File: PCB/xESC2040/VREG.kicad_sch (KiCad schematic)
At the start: 3 parts, among them U5 XC6220B331MR

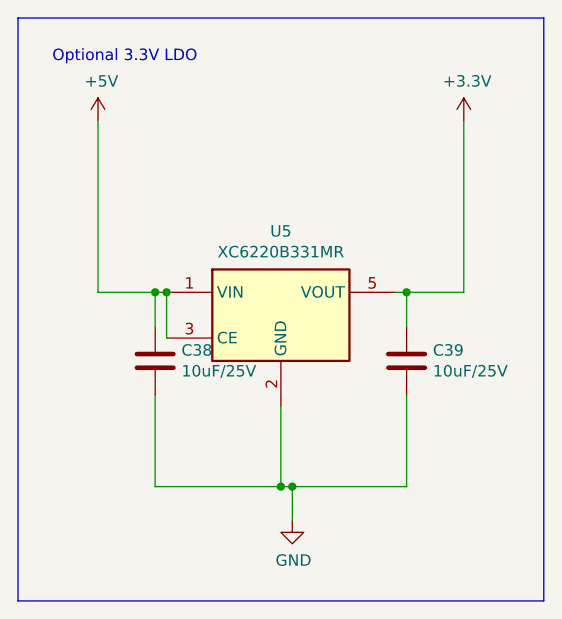
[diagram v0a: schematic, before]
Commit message: added CAN, WIP
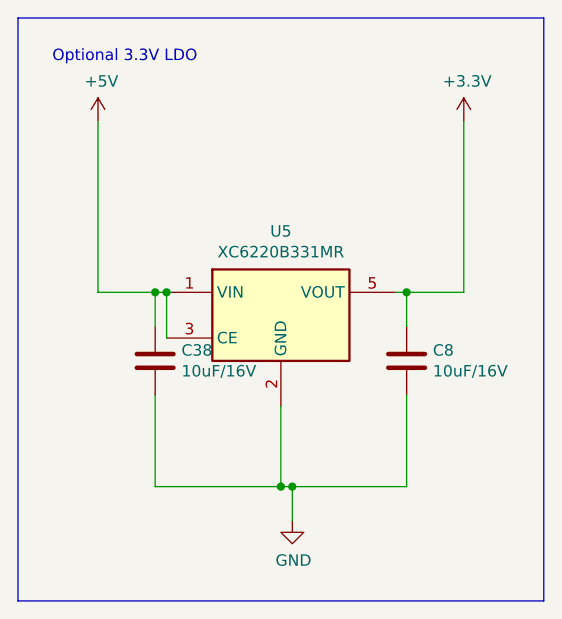
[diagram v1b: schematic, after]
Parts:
- removed C39: 10uF/25V, Capacitor_SMD:C_1206_3216Metric, symbol Device:C
- added C8: 10uF/16V, Capacitor_SMD:C_0603_1608Metric, symbol Device:C
- C38: value 10uF/25V -> 10uF/16V; footprint Capacitor_SMD:C_1206_3216Metric -> Capacitor_SMD:C_0603_1608Metric; Digikey 1276-1075-1-ND -> 1276-1096-2-ND; Part Number CL31A106KAHNNNE -> CL21A106KOQNNNE; Stock_PN C-1206-10uF-25V-X5R -> C-0603-10uF-16V
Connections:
- net +3V3: now also C8.1
- net GND: now also C8.2
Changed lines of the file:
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@@
       (effects (font (size 1.27 1.27)) (justify left))
     )
-    (property "Value" "10uF/25V" (id 1) (at 179.451 98.933 0)
+    (property "Value" "10uF/16V" (id 1) (at 179.451 98.933 0)
       (effects (font (size 1.27 1.27)) (justify left))
     )
-    (property "Footprint" "Capacitor_SMD:C_1206_3216Metric" (id 2) (at 177.4952 101.6 0)
+    (property "Footprint" "Capacitor_SMD:C_0603_1608Metric" (id 2) (at 177.4952 101.6 0)
       (effects (font (size 1.27 1.27)) hide)
     )
@@
       (effects (font (size 1.27 1.27)) hide)
     )
-    (property "Digikey" "1276-1075-1-ND" (id 4) (at 176.53 97.79 0)
+    (property "Digikey" "1276-1096-2-ND" (id 4) (at 176.53 97.79 0)
       (effects (font (size 1.27 1.27)) hide)
     )
-    (property "Part Number" "CL31A106KAHNNNE" (id 5) (at 176.53 97.79 0)
+    (property "Part Number" "CL21A106KOQNNNE" (id 5) (at 176.53 97.79 0)
       (effects (font (size 1.27 1.27)) hide)
     )
-    (property "Stock_PN" "C-1206-10uF-25V-X5R" (id 6) (at 176.53 97.79 0)
+    (property "Stock_PN" "C-0603-10uF-16V" (id 6) (at 176.53 97.79 0)
       (effects (font (size 1.27 1.27)) hide)
     )
@@
     )
     (pin "1")
-  )
-  (symbol (lib_id "Device:C") (at 204.47 97.79 0) (unit 1)
-    (in_bom yes) (on_board yes)
-    (property "Reference" "C39" (id 0) (at 207.391 96.6216 0)
-      (effects (font (size 1.27 1.27)) (justify left))
-    )
-    (property "Value" "10uF/25V" (id 1) (at 207.391 98.933 0)
-      (effects (font (size 1.27 1.27)) (justify left))
-    )
-    (property "Footprint" "Capacitor_SMD:C_1206_3216Metric" (id 2) (at 205.4352 101.6 0)
-      (effects (font (size 1.27 1.27)) hide)
-    )
-    (property "Datasheet" "~" (id 3) (at 204.47 97.79 0)
-      (effects (font (size 1.27 1.27)) hide)
-    )
-    (property "Digikey" "1276-1075-1-ND" (id 4) (at 204.47 97.79 0)
-      (effects (font (size 1.27 1.27)) hide)
-    )
-    (property "Part Number" "CL31A106KAHNNNE" (id 5) (at 204.47 97.79 0)
-      (effects (font (size 1.27 1.27)) hide)
-    )
-    (property "Stock_PN" "C-1206-10uF-25V-X5R" (id 6) (at 204.47 97.79 0)
-      (effects (font (size 1.27 1.27)) hide)
-    )
-    (pin "1")
-    (pin "2")
   )
   (symbol (lib_id "Regulator_Linear:XC6220B331MR") (at 190.5 92.71 0) (unit 1)
@@
     (pin "5")
   )
+  (symbol (lib_id "Device:C") (at 204.47 97.79 0) (unit 1)
+    (in_bom yes) (on_board yes)
+    (property "Reference" "C8" (id 0) (at 207.391 96.6216 0)
+      (effects (font (size 1.27 1.27)) (justify left))
+    )
+    (property "Value" "10uF/16V" (id 1) (at 207.391 98.933 0)
+      (effects (font (size 1.27 1.27)) (justify left))
+    )
+    (property "Footprint" "Capacitor_SMD:C_0603_1608Metric" (id 2) (at 205.4352 101.6 0)
+      (effects (font (size 1.27 1.27)) hide)
+    )
+    (property "Datasheet" "~" (id 3) (at 204.47 97.79 0)
+      (effects (font (size 1.27 1.27)) hide)
+    )
+    (property "Digikey" "1276-1096-2-ND" (id 4) (at 204.47 97.79 0)
+      (effects (font (size 1.27 1.27)) hide)
+    )
+    (property "Part Number" "CL21A106KOQNNNE" (id 5) (at 204.47 97.79 0)
+      (effects (font (size 1.27 1.27)) hide)
+    )
+    (property "Stock_PN" "C-0603-10uF-16V" (id 6) (at 204.47 97.79 0)
+      (effects (font (size 1.27 1.27)) hide)
+    )
+    (pin "1")
+    (pin "2")
+  )
 )

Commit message: Merge J5 and J1 into one connector - no pinout changes or connector move
With J5 gone had kicad redo  reference designators - hope that's ok
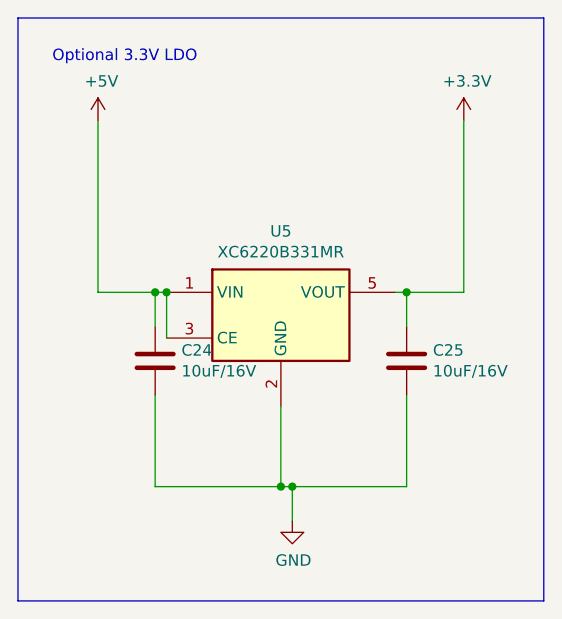
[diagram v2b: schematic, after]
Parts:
- renumbered C38 to C24, C8 to C25
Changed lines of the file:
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@@
   (symbol (lib_id "power:+3.3V") (at 210.82 71.12 0) (unit 1)
     (in_bom yes) (on_board yes)
-    (property "Reference" "#PWR038" (id 0) (at 210.82 74.93 0)
+    (property "Reference" "#PWR035" (id 0) (at 210.82 74.93 0)
       (effects (font (size 1.27 1.27)) hide)
     )
@@
   (symbol (lib_id "power:+5V") (at 170.18 71.12 0) (unit 1)
     (in_bom yes) (on_board yes)
-    (property "Reference" "#PWR036" (id 0) (at 170.18 74.93 0)
+    (property "Reference" "#PWR033" (id 0) (at 170.18 74.93 0)
       (effects (font (size 1.27 1.27)) hide)
     )
@@
   (symbol (lib_id "Device:C") (at 176.53 97.79 0) (unit 1)
     (in_bom yes) (on_board yes)
-    (property "Reference" "C38" (id 0) (at 179.451 96.6216 0)
+    (property "Reference" "C24" (id 0) (at 179.451 96.6216 0)
       (effects (font (size 1.27 1.27)) (justify left))
     )
@@
   (symbol (lib_id "power:GND") (at 191.77 115.57 0) (unit 1)
     (in_bom yes) (on_board yes)
-    (property "Reference" "#PWR037" (id 0) (at 191.77 121.92 0)
+    (property "Reference" "#PWR034" (id 0) (at 191.77 121.92 0)
       (effects (font (size 1.27 1.27)) hide)
     )
@@
   (symbol (lib_id "Device:C") (at 204.47 97.79 0) (unit 1)
     (in_bom yes) (on_board yes)
-    (property "Reference" "C8" (id 0) (at 207.391 96.6216 0)
+    (property "Reference" "C25" (id 0) (at 207.391 96.6216 0)
       (effects (font (size 1.27 1.27)) (justify left))
     )

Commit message: wip
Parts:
- C24, C25: value 10uF/16V -> 4.7uF/16V
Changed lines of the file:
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@@
       (effects (font (size 1.27 1.27)) (justify left))
     )
-    (property "Value" "10uF/16V" (id 1) (at 179.451 98.933 0)
+    (property "Value" "4.7uF{slash}16V" (id 1) (at 179.451 98.933 0)
       (effects (font (size 1.27 1.27)) (justify left))
     )
@@
       (effects (font (size 1.27 1.27)) (justify left))
     )
-    (property "Value" "10uF/16V" (id 1) (at 207.391 98.933 0)
+    (property "Value" "4.7uF{slash}16V" (id 1) (at 207.391 98.933 0)
       (effects (font (size 1.27 1.27)) (justify left))
     )

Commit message: updated wrong BOM part number
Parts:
- U5: LCSC C73336 -> C86534
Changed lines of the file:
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@@
       (effects (font (size 1.27 1.27)) hide)
     )
-    (property "LCSC" "C73336" (id 6) (at 190.5 92.71 0)
+    (property "LCSC" "C86534" (id 6) (at 190.5 92.71 0)
       (effects (font (size 1.27 1.27)) hide)
     )
